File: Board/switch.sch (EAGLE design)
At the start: 31 parts, among them IC1 MCP2300X/SO, IC2 LM1117, U1 ADS1015

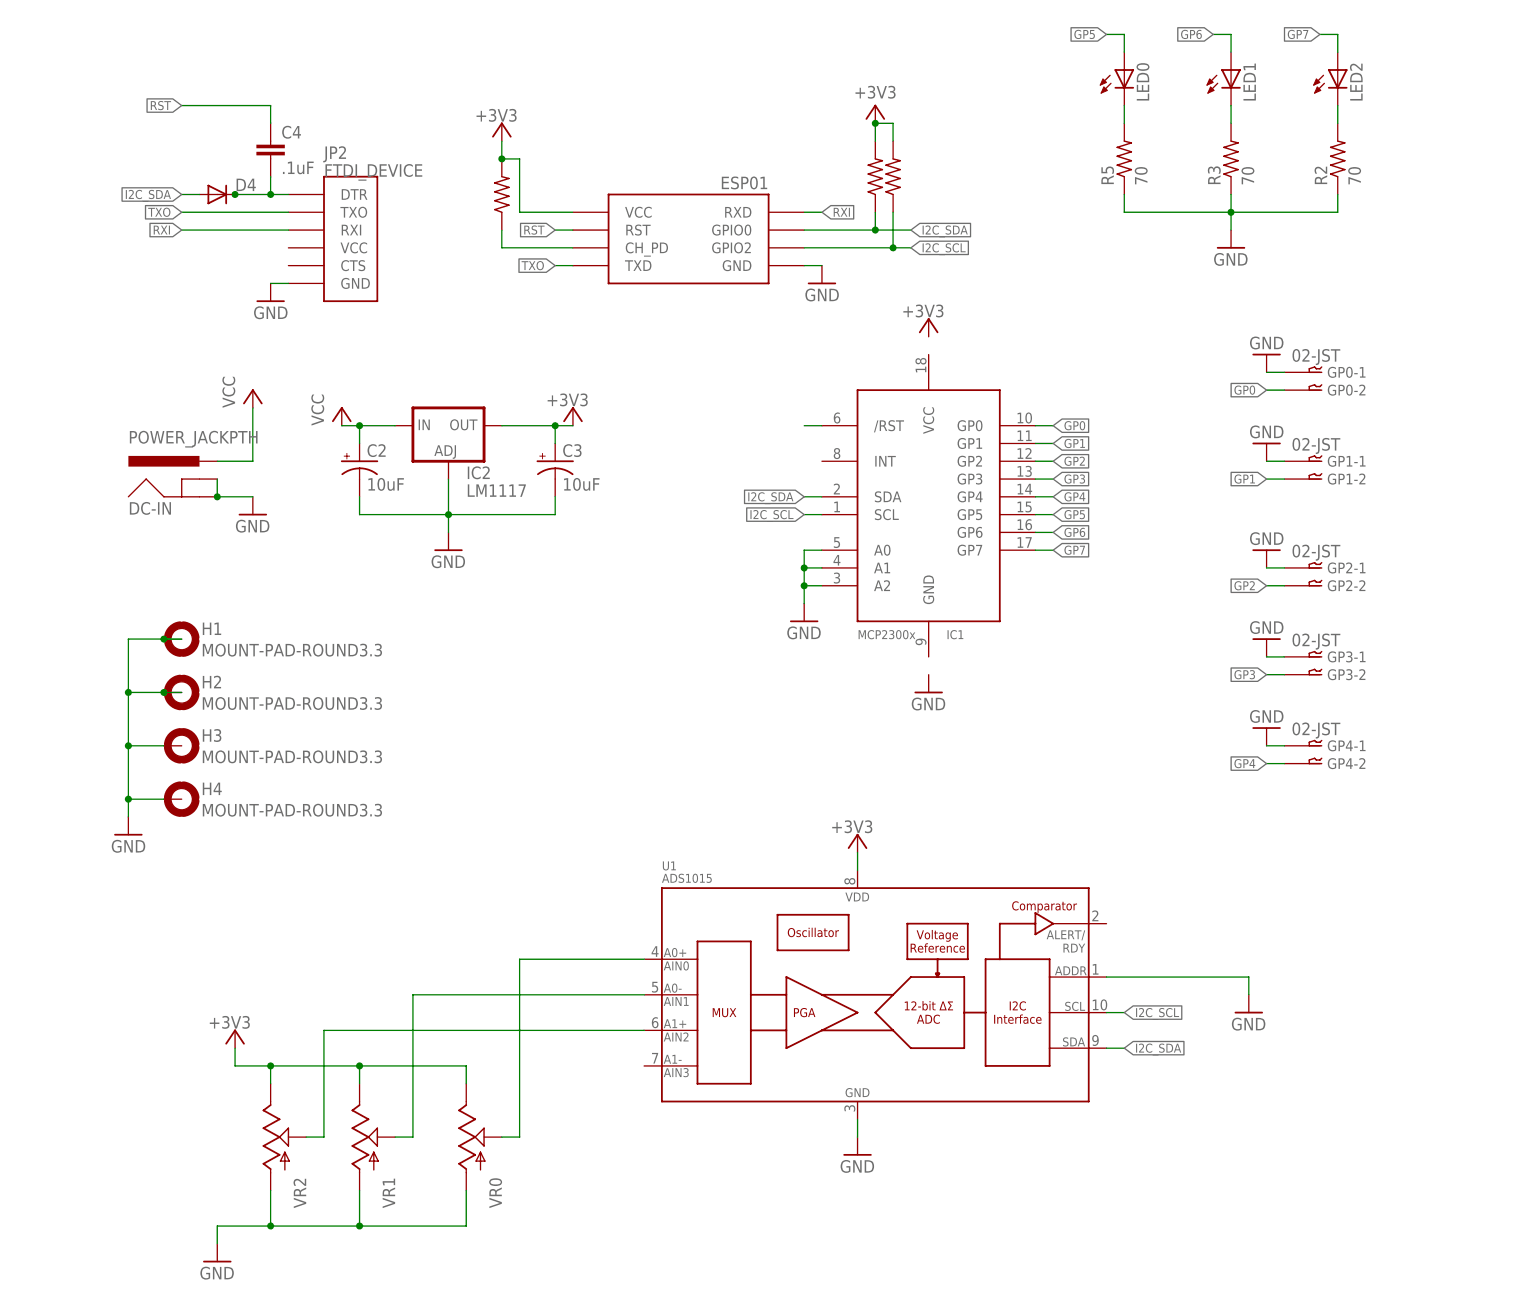
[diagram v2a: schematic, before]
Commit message: Use pcb-mount buttons
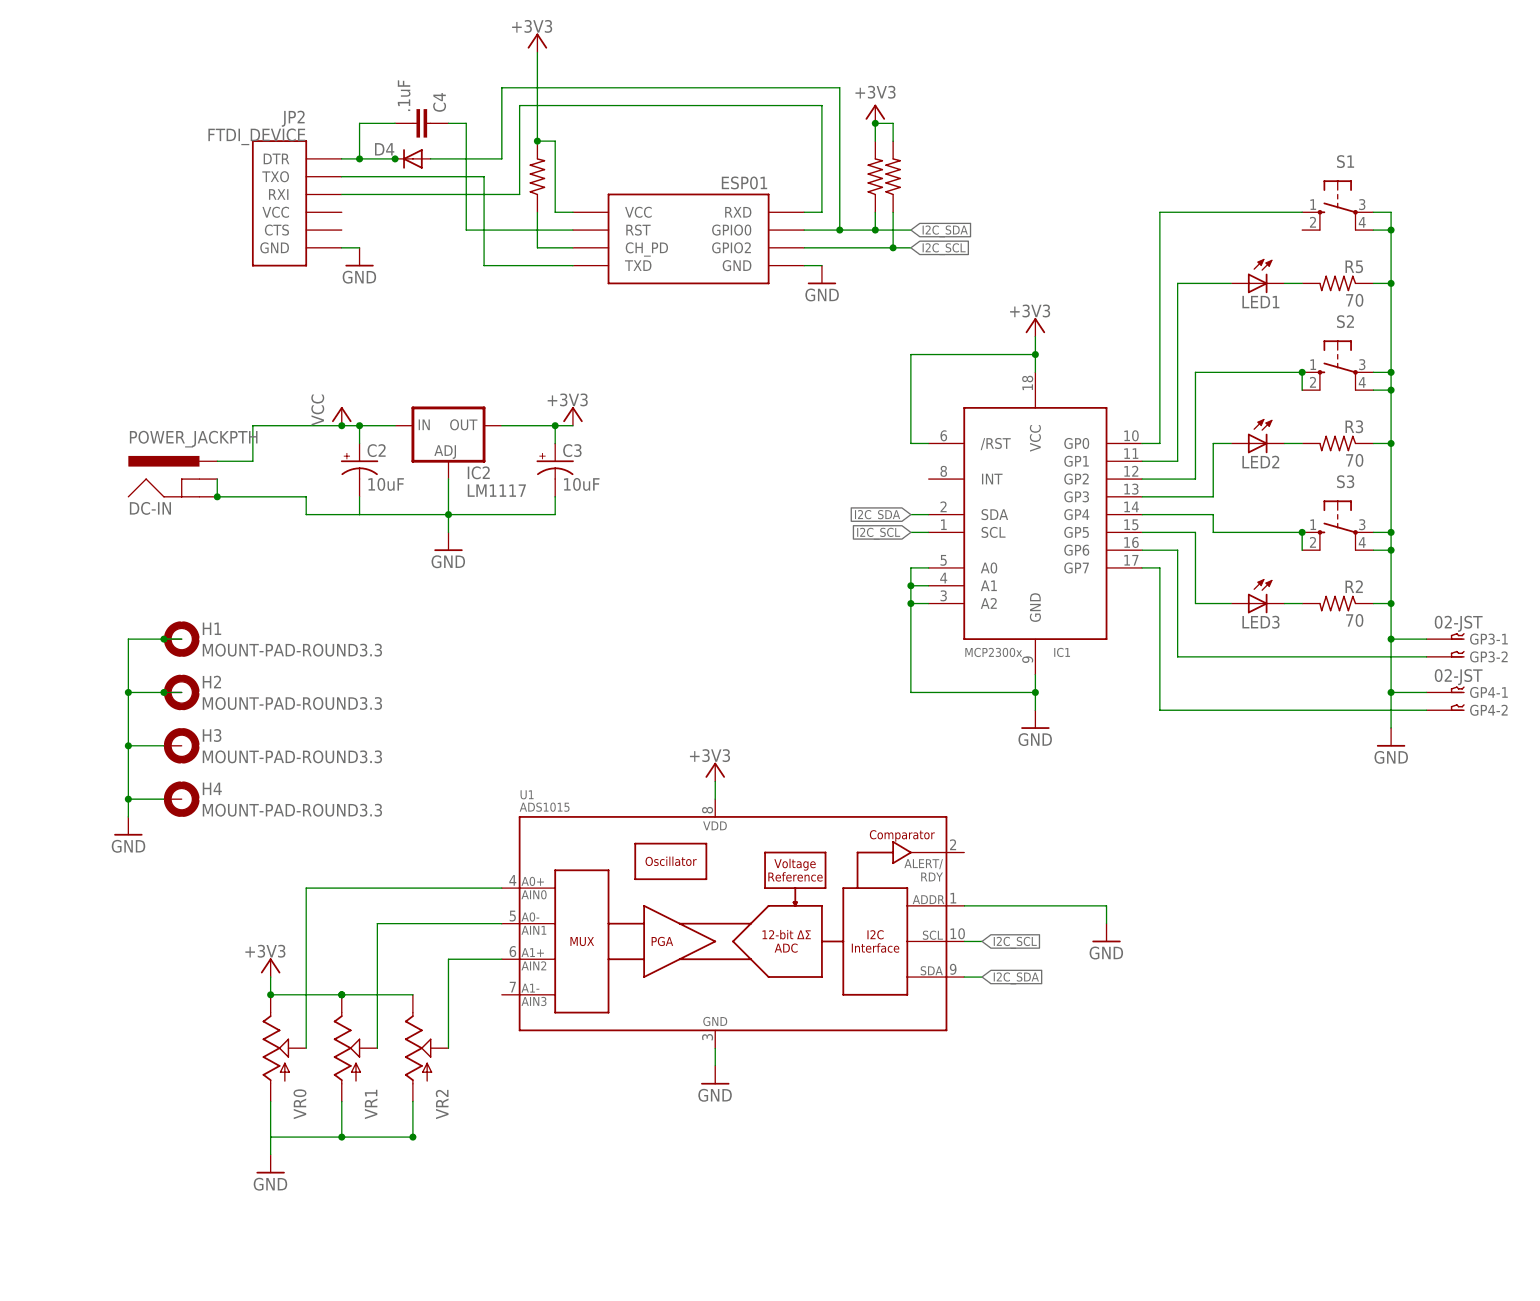
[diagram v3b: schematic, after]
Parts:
- removed GP0, GP1, GP2: 02-JST, con-jst-xh:02-JST
- removed LED0: (no value), adafruit:LED3MM
- added LED3: (no value), adafruit:LED3MM
- added S1, S2, S3: (no value), switch-omron:10-XX
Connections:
- removed net DSD: GP2-1.1
- removed net N$11: IC1./RST
- new net N$9: DC-IN.GND, DC-IN.GNDBREAK
- net +3V3: now also IC1./RST, IC1.VCC
- net GND: now also IC1.GND, S1.P, S1.P1, S2.P, S2.P1, S3.P, S3.P1; no longer DC-IN.GND, DC-IN.GNDBREAK, GP0-1.1, GP1-1.1
- net GP0: now also S1.S; no longer GP0-2.1
- net GP1: now also LED1.A; no longer GP1-2.1
- net GP2: now also S2.S, S2.S1; no longer GP2-2.1
- net GP3: now also LED2.A; no longer GP3-2.1
- net GP4: now also S3.S, S3.S1; no longer GP4-2.1
- net GP5: now also LED3.A; no longer LED0.A
- net GP6: now also GP3-2.1; no longer LED1.A
- net GP7: now also GP4-2.1; no longer LED2.A
- net N$6: now also LED1.C; no longer LED0.C
- net N$7: now also LED2.C; no longer LED1.C
- net N$8: now also LED3.C; no longer LED2.C
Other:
- moved on the sheet: C4, D4, GP3-1, GP3-2, GP4-1, GP4-2, IC1, JP2, LED1, LED2, R2, R3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

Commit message: Route traces and tweak layout
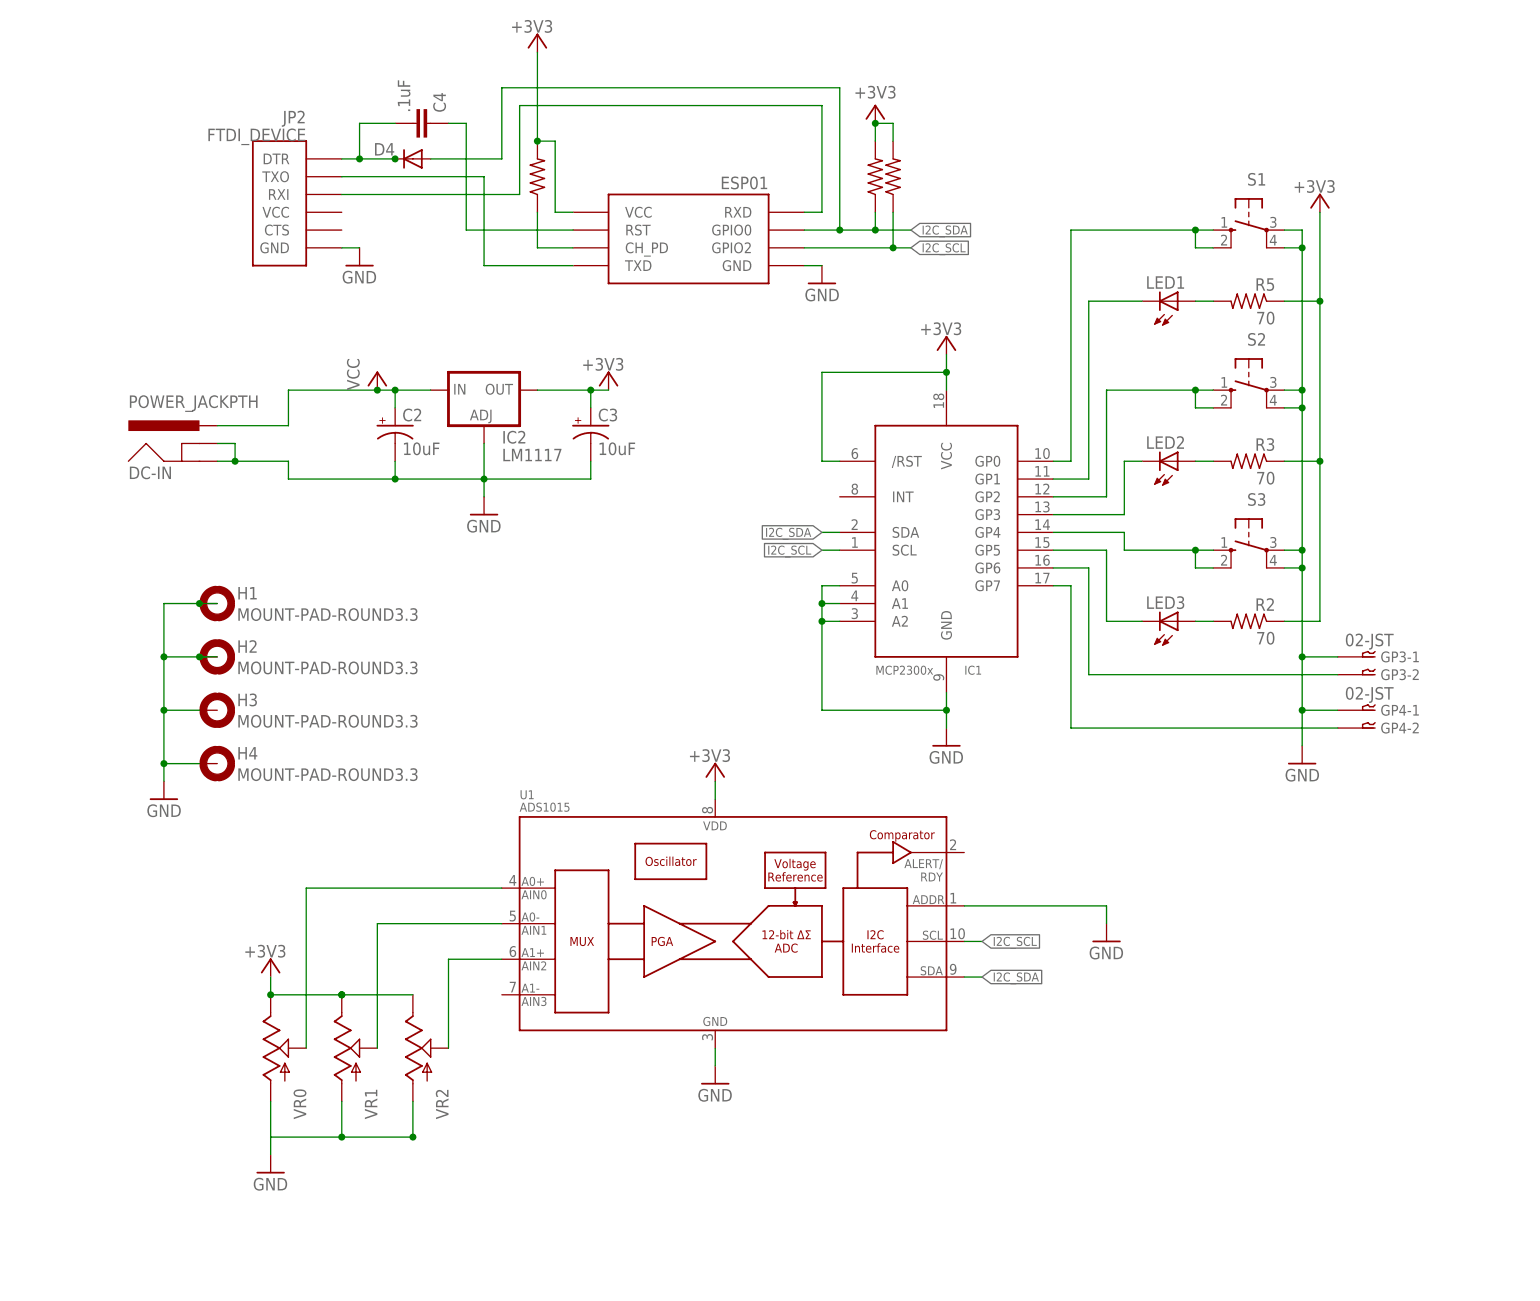
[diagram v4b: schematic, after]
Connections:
- removed net N$7: LED2.C, R3.2
- removed net N$9: DC-IN.GND, DC-IN.GNDBREAK
- new net N$10: LED3.A, R2.2
- net +3V3: now also R2.1, R3.1, R5.1
- net GND: now also DC-IN.GND, DC-IN.GNDBREAK; no longer R2.1, R3.1, R5.1
- net GP0: now also S1.S1
- net GP1: now also LED1.C; no longer LED1.A
- net GP3: now also LED2.C; no longer LED2.A
- net GP5: now also LED3.C; no longer LED3.A
- net N$6: now also LED1.A; no longer LED1.C
- net N$8: now also LED2.A, R3.2; no longer LED3.C, R2.2
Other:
- moved on the sheet: C2, C3, DC-IN, GP3-1, GP3-2, GP4-1, GP4-2, H1, H2, H3, H4, IC1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
